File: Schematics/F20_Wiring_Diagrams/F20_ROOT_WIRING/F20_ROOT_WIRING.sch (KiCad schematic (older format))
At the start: 0 parts

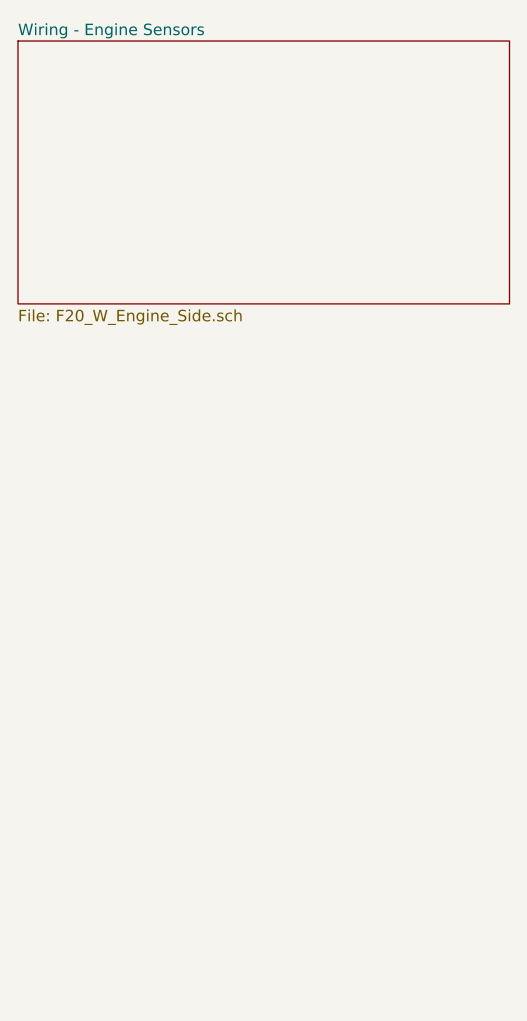
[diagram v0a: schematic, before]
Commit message: Added engine side shifter wiring. Started engine side power management wiring
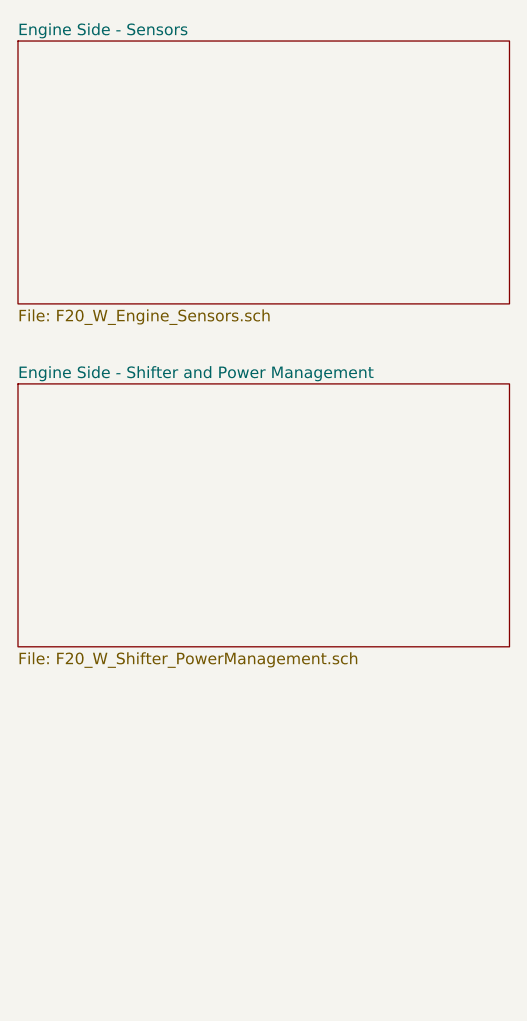
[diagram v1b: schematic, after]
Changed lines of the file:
@@
 $Descr A 11000 8500
 encoding utf-8
-Sheet 1 2
+Sheet 1 3
 Title "Root - Wiring"
 Date "2020-03-12"
@@
 S 1500 1000 2150 1150
 U 5E6ACFA6
-F0 "Wiring - Engine Sensors" 50
-F1 "F20_W_Engine_Side.sch" 50
+F0 "Engine Side - Sensors" 50
+F1 "F20_W_Engine_Sensors.sch" 50
+$EndSheet
+$Sheet
+S 1500 2500 2150 1150
+U 5EF123F4
+F0 "Engine Side - Shifter and Power Management" 50
+F1 "F20_W_Shifter_PowerManagement.sch" 50
 $EndSheet
 $EndSCHEMATC

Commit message: Added shifter, brake light wiring, organized pwr mgmt diagrams
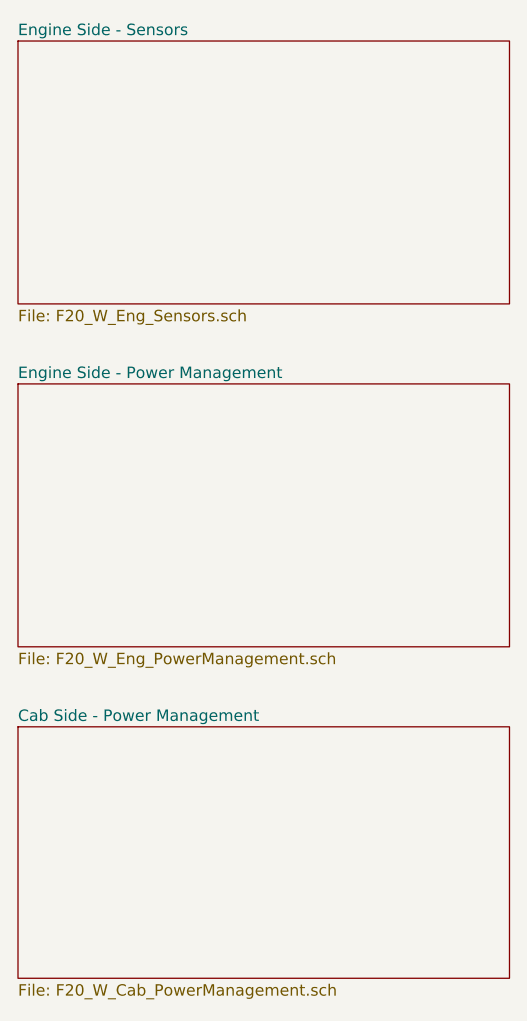
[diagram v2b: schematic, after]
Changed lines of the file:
@@
 $Descr A 11000 8500
 encoding utf-8
-Sheet 1 3
+Sheet 1 4
 Title "Root - Wiring"
 Date "2020-03-12"
@@
 $EndDescr
 $Sheet
+S 1500 4000 2150 1100
+U 5F84BCE1
+F0 "Cab Side - Power Management" 50
+F1 "F20_W_Cab_PowerManagement.sch" 50
+$EndSheet
+$Sheet
 S 1500 1000 2150 1150
 U 5E6ACFA6
 F0 "Engine Side - Sensors" 50
-F1 "F20_W_Engine_Sensors.sch" 50
+F1 "F20_W_Eng_Sensors.sch" 50
 $EndSheet
 $Sheet
 S 1500 2500 2150 1150
 U 5EF123F4
-F0 "Engine Side - Shifter and Power Management" 50
-F1 "F20_W_Shifter_PowerManagement.sch" 50
+F0 "Engine Side - Power Management" 50
+F1 "F20_W_Eng_PowerManagement.sch" 50
 $EndSheet
 $EndSCHEMATC
